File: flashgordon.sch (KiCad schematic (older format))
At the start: 3 parts

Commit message: draw circuit
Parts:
- removed P?: RS232, symbol CONN_01X09
- removed P?: SPI, symbol CONN_01X06
- added 2.2K: R, symbol R
- added C? (x2): 27pF, symbol C
- added C?: 3.3uF, symbol C
- added C? (x7): 100nF, symbol C
- added P?: USB_OTG, symbol USB_OTG
- added P?: SPI-Clip, symbol SPI-Clip
- added R?: 12K, symbol R
- added R?: 1K, symbol R
- added R?: 10K, symbol R
- added U?: 3.3V_Voltage_Regulator, symbol 3.3V_Voltage_Regulator
- added U?: 93CxxC, symbol 93CxxC
- added Y?: 12MHz, symbol Crystal
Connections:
- net labels added: +3.3V, DM, DP, GND, VCORE
- wire segments 0 -> 112
- no-connect marks 0 -> 8
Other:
- moved on the sheet: U?

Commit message: add LM2596
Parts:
- removed U?: 3.3V_Voltage_Regulator, symbol 3.3V_Voltage_Regulator
- added U?: LM2596S-3.3, TO-263-5, symbol LM2596S-3.3
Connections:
- net labels added: +24V
- wire segments 112 -> 118
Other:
- moved on the sheet: P?
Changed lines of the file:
@@
 LIBS:flashgordon
 LIBS:spi-clip
+LIBS:dc-dc
 LIBS:flashgordon-cache
 EELAYER 25 0
@@
 $Comp
 L +3.3V #PWR?
-U 1 1 57B8F89A
-P 3500 2100
-F 0 "#PWR?" H 3500 1950 50  0001 C CNN
-F 1 "+3.3V" H 3500 2240 50  0000 C CNN
-F 2 "" H 3500 2100 50  0000 C CNN
-F 3 "" H 3500 2100 50  0000 C CNN
-	1    3500 2100
-	1    0    0    -1
-$EndComp
-$Comp
-L +3.3V #PWR?
 U 1 1 57B8FB97
 P 6250 3800
@@
 $EndComp
 $Comp
-L +3.3V #PWR?
-U 1 1 57B922AF
-P 3150 2100
-F 0 "#PWR?" H 3150 1950 50  0001 C CNN
-F 1 "+3.3V" H 3150 2240 50  0000 C CNN
-F 2 "" H 3150 2100 50  0000 C CNN
-F 3 "" H 3150 2100 50  0000 C CNN
-	1    3150 2100
-	1    0    0    -1
-$EndComp
-$Comp
 L C C?
 U 1 1 57B925FD
@@
 $EndComp
 $Comp
-L 3.3V_Voltage_Regulator U?
-U 1 1 57B9E519
-P 2300 1700
-F 0 "U?" H 2050 1700 60  0000 C CNN
-F 1 "3.3V_Voltage_Regulator" H 2300 2050 60  0000 C CNN
-F 2 "" H 2300 1700 60  0000 C CNN
-F 3 "" H 2300 1700 60  0000 C CNN
-	1    2300 1700
-	0    1    1    0
-$EndComp
-$Comp
 L USB_OTG P?
 U 1 1 57B9E60C
-P 1400 1700
-F 0 "P?" H 1725 1575 50  0000 C CNN
-F 1 "USB_OTG" H 1400 1900 50  0000 C CNN
-F 2 "" V 1350 1600 50  0000 C CNN
-F 3 "" V 1350 1600 50  0000 C CNN
-	1    1400 1700
+P 8100 5700
+F 0 "P?" H 8425 5575 50  0000 C CNN
+F 1 "USB_OTG" H 8100 5900 50  0000 C CNN
+F 2 "" V 8050 5600 50  0000 C CNN
+F 3 "" V 8050 5600 50  0000 C CNN
+	1    8100 5700
 	0    -1   -1   0
 $EndComp
@@
 L +3.3V #PWR?
 U 1 1 57B9E84F
-P 2100 1300
-F 0 "#PWR?" H 2100 1150 50  0001 C CNN
-F 1 "+3.3V" H 2100 1440 50  0000 C CNN
-F 2 "" H 2100 1300 50  0000 C CNN
-F 3 "" H 2100 1300 50  0000 C CNN
-	1    2100 1300
-	1    0    0    -1
-$EndComp
-Text Label 1750 1700 0    60   ~ 0
+P 10900 5050
+F 0 "#PWR?" H 10900 4900 50  0001 C CNN
+F 1 "+3.3V" H 10900 5190 50  0000 C CNN
+F 2 "" H 10900 5050 50  0000 C CNN
+F 3 "" H 10900 5050 50  0000 C CNN
+	1    10900 5050
+	1    0    0    -1
+$EndComp
+Text Label 8450 5700 0    60   ~ 0
 DP
-Text Label 1750 1800 0    60   ~ 0
+Text Label 8450 5800 0    60   ~ 0
 DM
 Text Label 4200 3200 2    60   ~ 0
@@
 Text Label 4200 3300 2    60   ~ 0
 DP
-NoConn ~ 1700 1600
-NoConn ~ 1300 1250
+NoConn ~ 8400 5600
+NoConn ~ 8000 5250
 $Comp
 L +3.3V #PWR?
@@
 	6500 1800 6500 1950
 Wire Wire Line
-	1300 1300 1300 1250
-Wire Wire Line
-	1700 1500 1900 1500
-Wire Wire Line
-	1900 1500 1900 1600
-Wire Wire Line
-	1900 1600 2100 1600
-Wire Wire Line
-	2100 1700 2100 1300
-Wire Wire Line
-	2100 1800 1900 1800
-Wire Wire Line
-	1900 1800 1900 1900
-Wire Wire Line
-	1900 1900 1700 1900
-Wire Wire Line
-	1700 1700 1750 1700
-Wire Wire Line
-	1700 1800 1750 1800
+	8000 5300 8000 5250
+Wire Wire Line
+	8400 5500 8600 5500
+Wire Wire Line
+	8600 5500 8600 5600
+Wire Wire Line
+	8600 5600 8800 5600
+Wire Wire Line
+	8800 5800 8600 5800
+Wire Wire Line
+	8600 5800 8600 5900
+Wire Wire Line
+	8600 5900 8400 5900
+Wire Wire Line
+	8400 5700 8450 5700
+Wire Wire Line
+	8400 5800 8450 5800
 Wire Wire Line
 	4200 3200 4350 3200
@@
 Wire Wire Line
 	2100 4750 2500 4750
+$Comp
+L LM2596S-3.3 U?
+U 1 1 57C212CC
+P 9900 5100
+F 0 "U?" H 9500 5450 50  0000 L CNN
+F 1 "LM2596S-3.3" H 9500 5350 50  0000 L CNN
+F 2 "TO-263-5" H 10200 4850 50  0000 C CIN
+F 3 "" H 9900 5100 50  0000 C CNN
+	1    9900 5100
+	1    0    0    -1
+$EndComp
+$Comp
+L +24V #PWR?
+U 1 1 57C22116
+P 9200 4750
+F 0 "#PWR?" H 9200 4600 50  0001 C CNN
+F 1 "+24V" H 9200 4890 50  0000 C CNN
+F 2 "" H 9200 4750 50  0000 C CNN
+F 3 "" H 9200 4750 50  0000 C CNN
+	1    9200 4750
+	1    0    0    -1
+$EndComp
+Wire Wire Line
+	9200 4750 9200 5000
+Wire Wire Line
+	9200 5000 9400 5000
+$Comp
+L GND #PWR?
+U 1 1 57C22CDF
+P 9200 5600
+F 0 "#PWR?" H 9200 5350 50  0001 C CNN
+F 1 "GND" H 9200 5450 50  0000 C CNN
+F 2 "" H 9200 5600 50  0000 C CNN
+F 3 "" H 9200 5600 50  0000 C CNN
+	1    9200 5600
+	1    0    0    -1
+$EndComp
+Wire Wire Line
+	9400 5200 9200 5200
+Wire Wire Line
+	9200 5200 9200 5600
+$Comp
+L GND #PWR?
+U 1 1 57C22F2B
+P 9900 5600
+F 0 "#PWR?" H 9900 5350 50  0001 C CNN
+F 1 "GND" H 9900 5450 50  0000 C CNN
+F 2 "" H 9900 5600 50  0000 C CNN
+F 3 "" H 9900 5600 50  0000 C CNN
+	1    9900 5600
+	1    0    0    -1
+$EndComp
+Wire Wire Line
+	9900 5400 9900 5600
+Wire Wire Line
+	10400 5200 10900 5200
+Wire Wire Line
+	10900 5200 10900 5050
 $EndSCHEMATC

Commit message: basic schematic done
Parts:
- added 1N5824: D, symbol D
- added 220uF, 680uF: C, symbol C
- added JP?: JUMPER3, symbol JUMPER3
- added L?: INDUCTOR, symbol INDUCTOR
- gave numbers to parts that had none: 19
- renumbered 2.2K to 2.2K1
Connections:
- wire segments 118 -> 126
- no-connect marks 8 -> 36
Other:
- moved on the sheet: 2.2K1, C1, C10, C2, C3, C4, C5, C6, C7, C8, C9, P1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

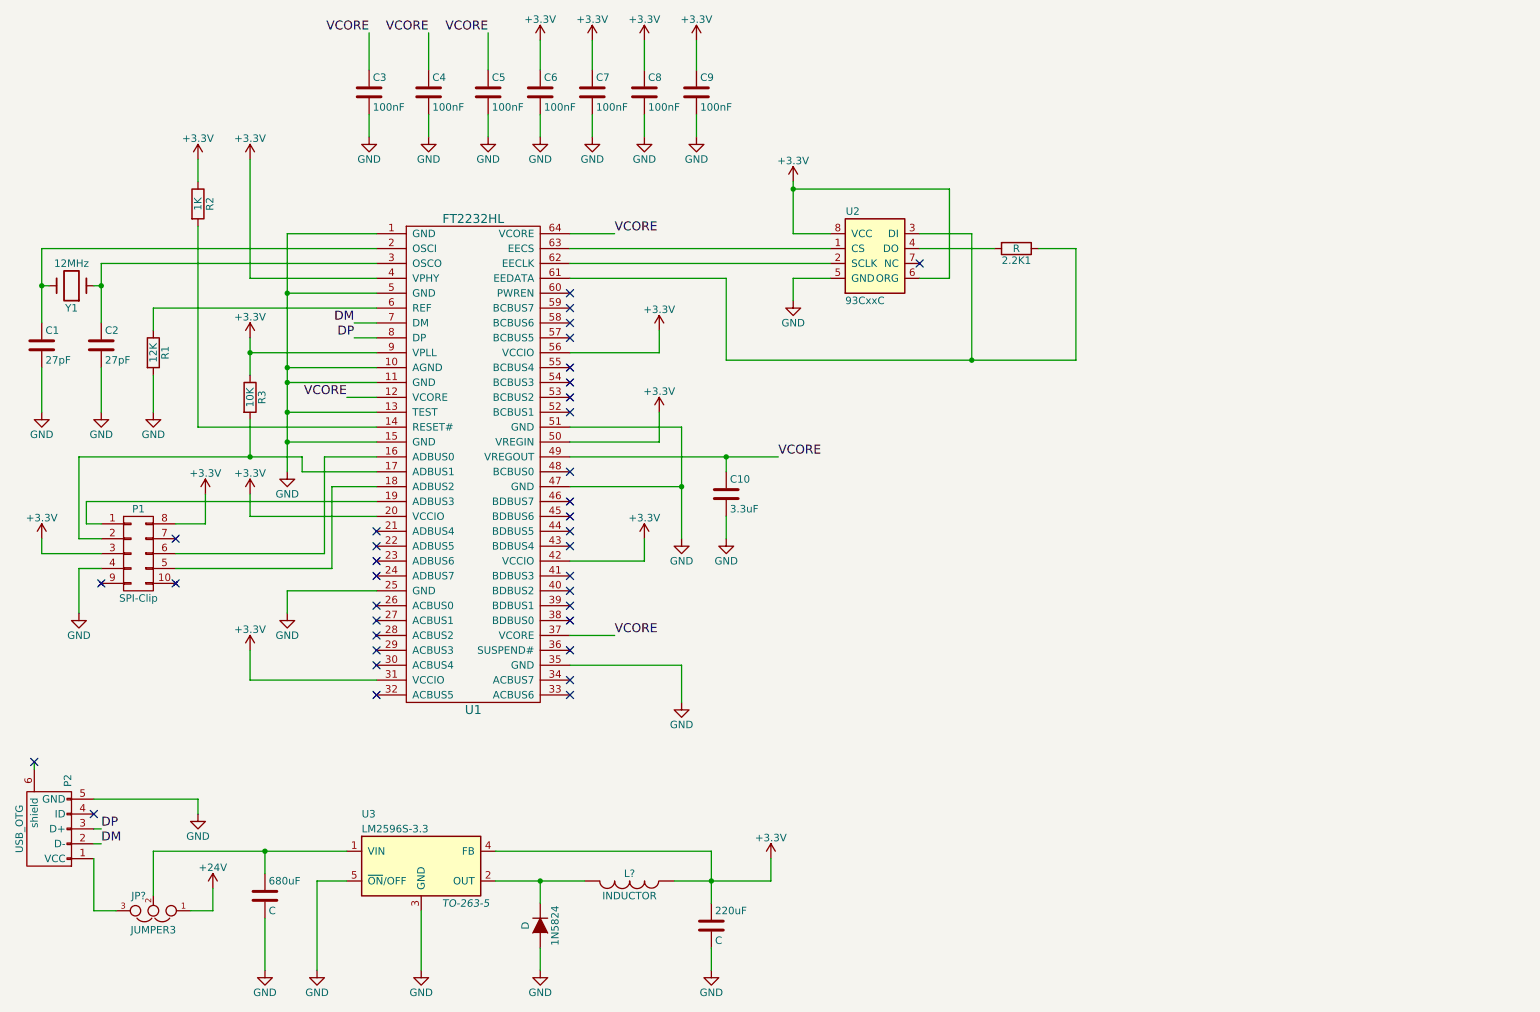
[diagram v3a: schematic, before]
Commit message: add basic pcb
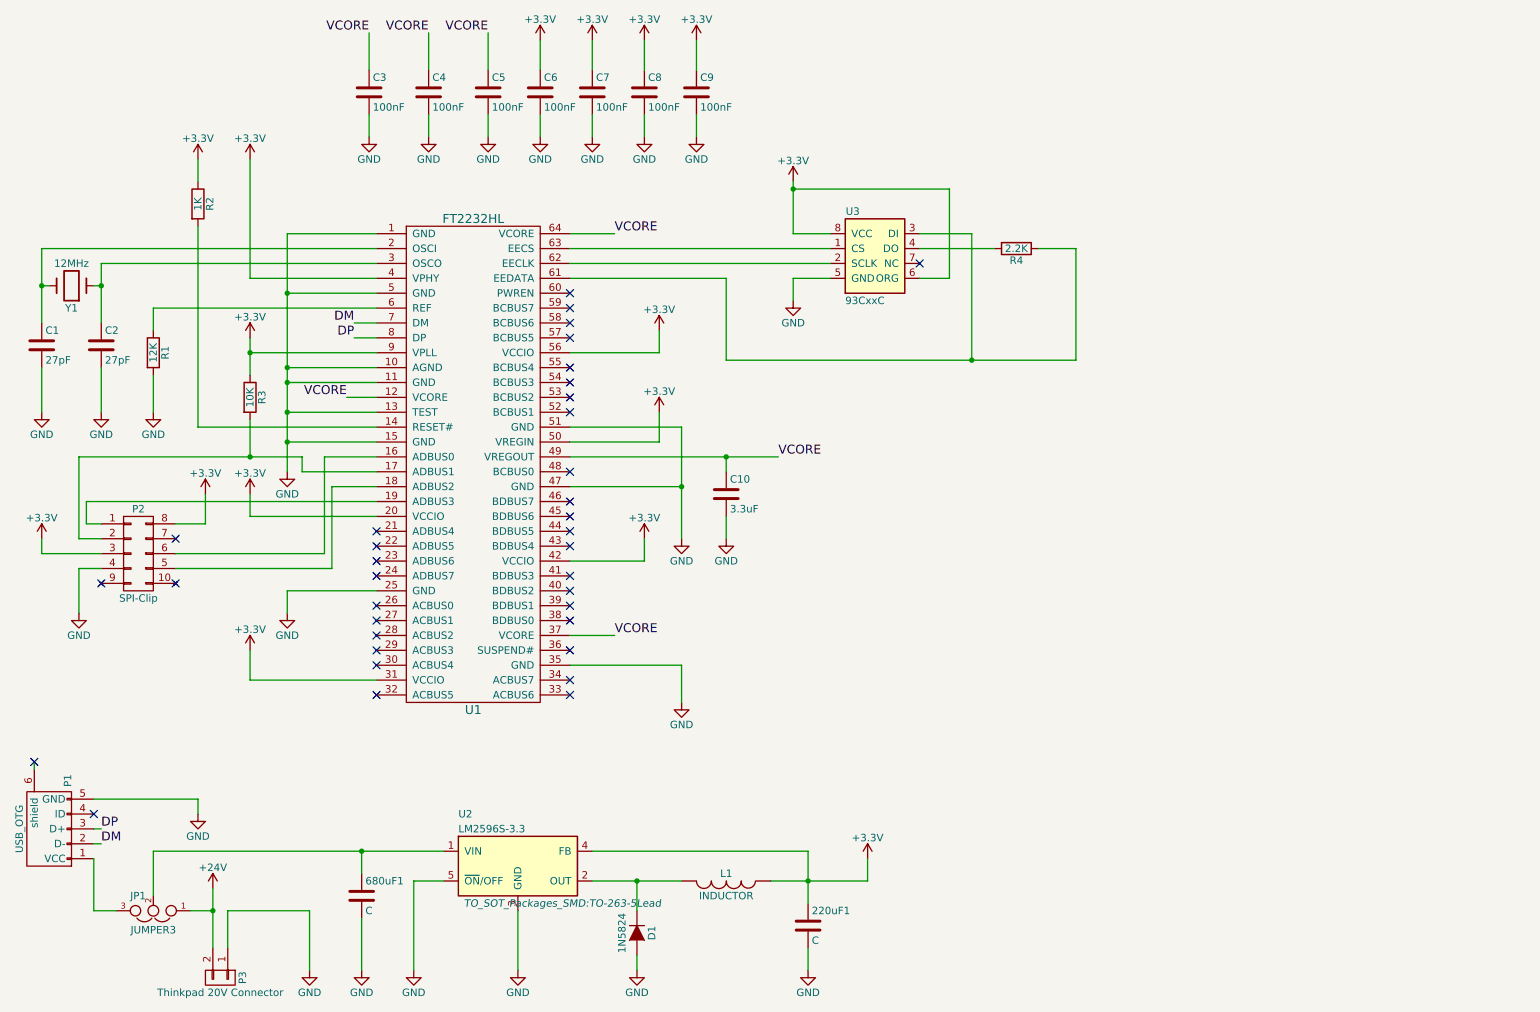
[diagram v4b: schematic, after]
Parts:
- removed 1N5824: D, symbol D
- removed P1: SPI-Clip, symbol SPI-Clip
- added D1: 1N5824, Diodes_ThroughHole:Diode_DO-35_SOD27_Horizontal_RM10, symbol 1N5824
- added P2: SPI-Clip, Pin_Headers:Pin_Header_Straight_2x05, symbol SPI-Clip
- added P3: Thinkpad 20V Connector, Terminal_Blocks:TerminalBlock_Pheonix_MKDS1.5-2pol, symbol CONN_01X02
- 220uF1: renamed from 220uF; footprint (none) -> Capacitors_ThroughHole:C_Radial_D5_L6_P2.5
- 680uF1: renamed from 680uF; footprint (none) -> Capacitors_ThroughHole:C_Radial_D5_L6_P2.5
- C1, C2: footprint (none) -> Capacitors_ThroughHole:C_Disc_D3_P2.5
- C10, C3, C4, C5, C6, C7, C8, C9: footprint (none) -> Capacitors_SMD:C_0805
- JP1: renamed from JP?; footprint (none) -> Pin_Headers:Pin_Header_Straight_1x03
- L1: renamed from L?; footprint (none) -> Choke_SMD:Choke_SMD_12x12mm_h8mm
- P1: renamed from P2; footprint (none) -> Connect:USB_Micro-B
- R1, R2, R3: footprint (none) -> Resistors_SMD:R_0805
- R4: renamed from 2.2K1; value R -> 2.2K; footprint (none) -> Resistors_SMD:R_0805
- U1: footprint (none) -> Housings_QFP:LQFP-64_10x10mm_Pitch0.5mm
- U2: renamed from U3; footprint TO-263-5 -> TO_SOT_Packages_SMD:TO-263-5Lead
- U3: renamed from U2; footprint (none) -> Housings_SOIC:SOIC-8_3.9x4.9mm_Pitch1.27mm
- Y1: footprint (none) -> Crystals:Crystal_HC50-U_Vertical
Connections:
- net +24V: now also P3.2 (P2)
- net +3V3: now also P2.3 (P5), P2.8 (P2)
- net GND: now also D1.2 (A), P2.4 (P7), P3.1 (P1)
- net at U1.16 (ADBUS0): now also P2.6 (P6)
- net at R3.2, U1.17 (ADBUS1): now also P2.2 (P3)
- net at U1.18 (ADBUS2): now also P2.5 (P8)
- net at U1.19 (ADBUS3): now also P2.1 (P1)
- net at L1.2, U2.2 (OUT): now also D1.1 (K)
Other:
- moved on the sheet: 220uF1, 680uF1, L1, U2
